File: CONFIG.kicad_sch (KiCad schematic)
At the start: 26 parts, among them IC1 ECP5-BGA256, J1 Conn_ARM_JTAG_SWD_10, U5 AT25SF081-SSHD-X

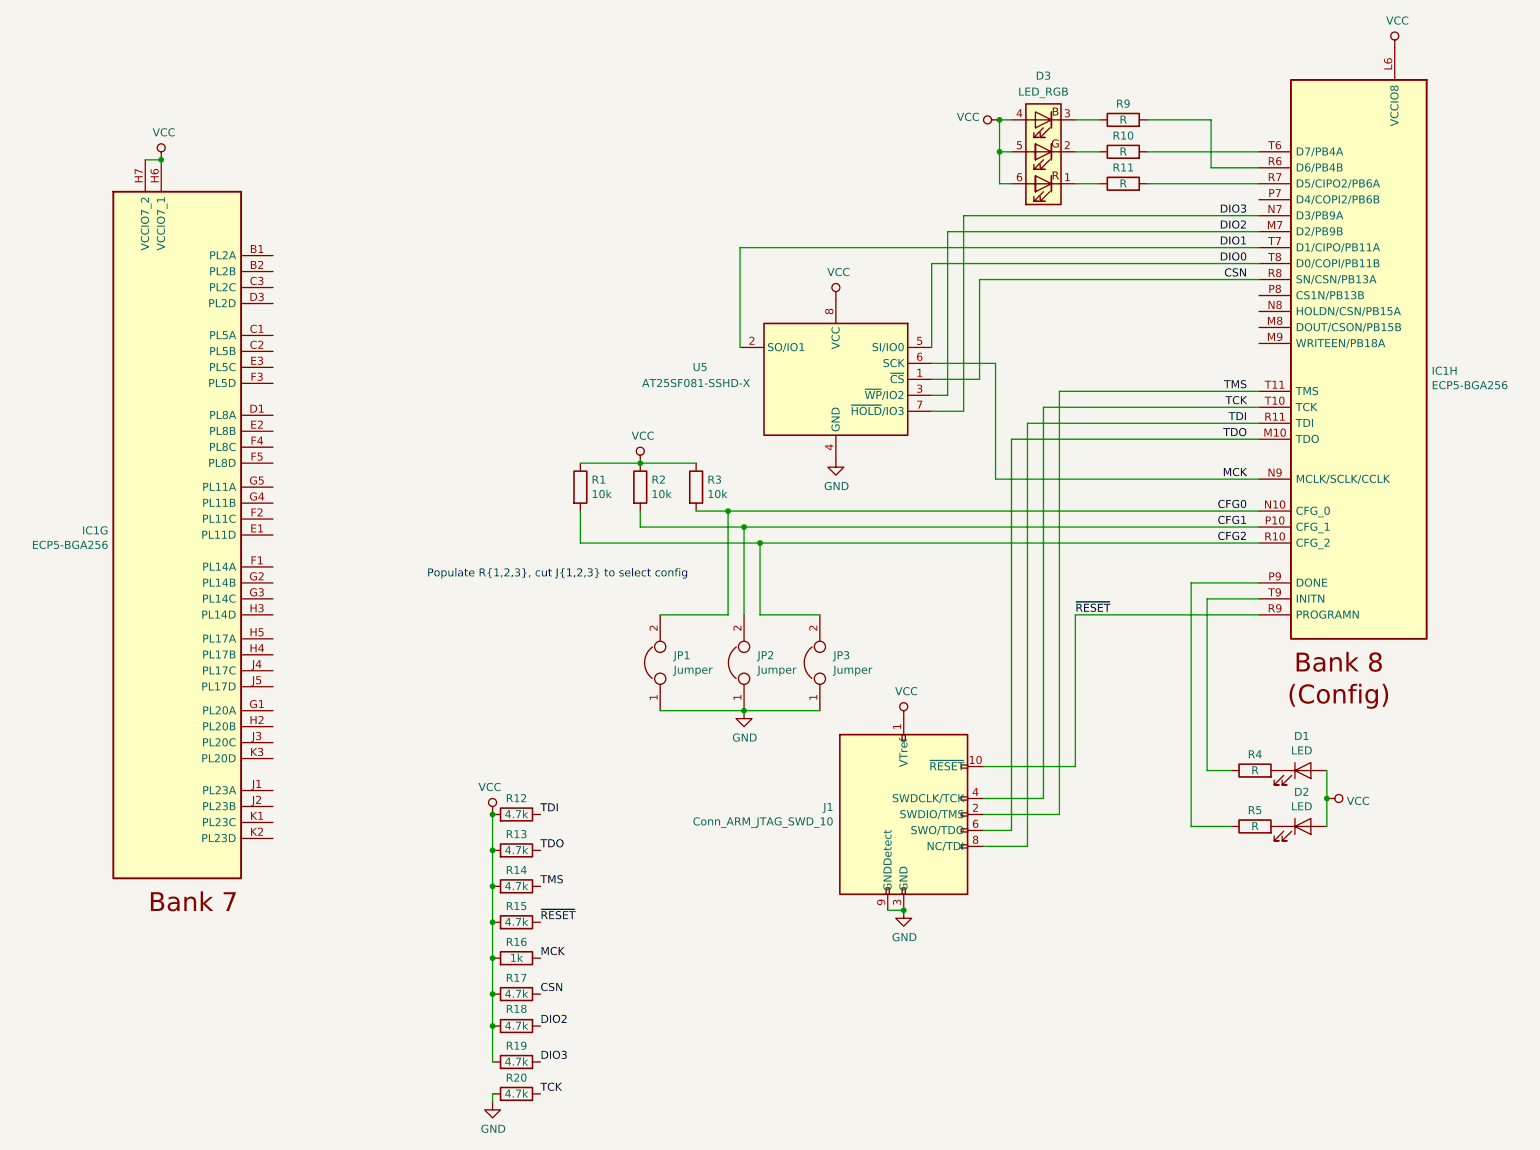
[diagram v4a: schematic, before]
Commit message: Change oscillator to SI5315, change RGB LED
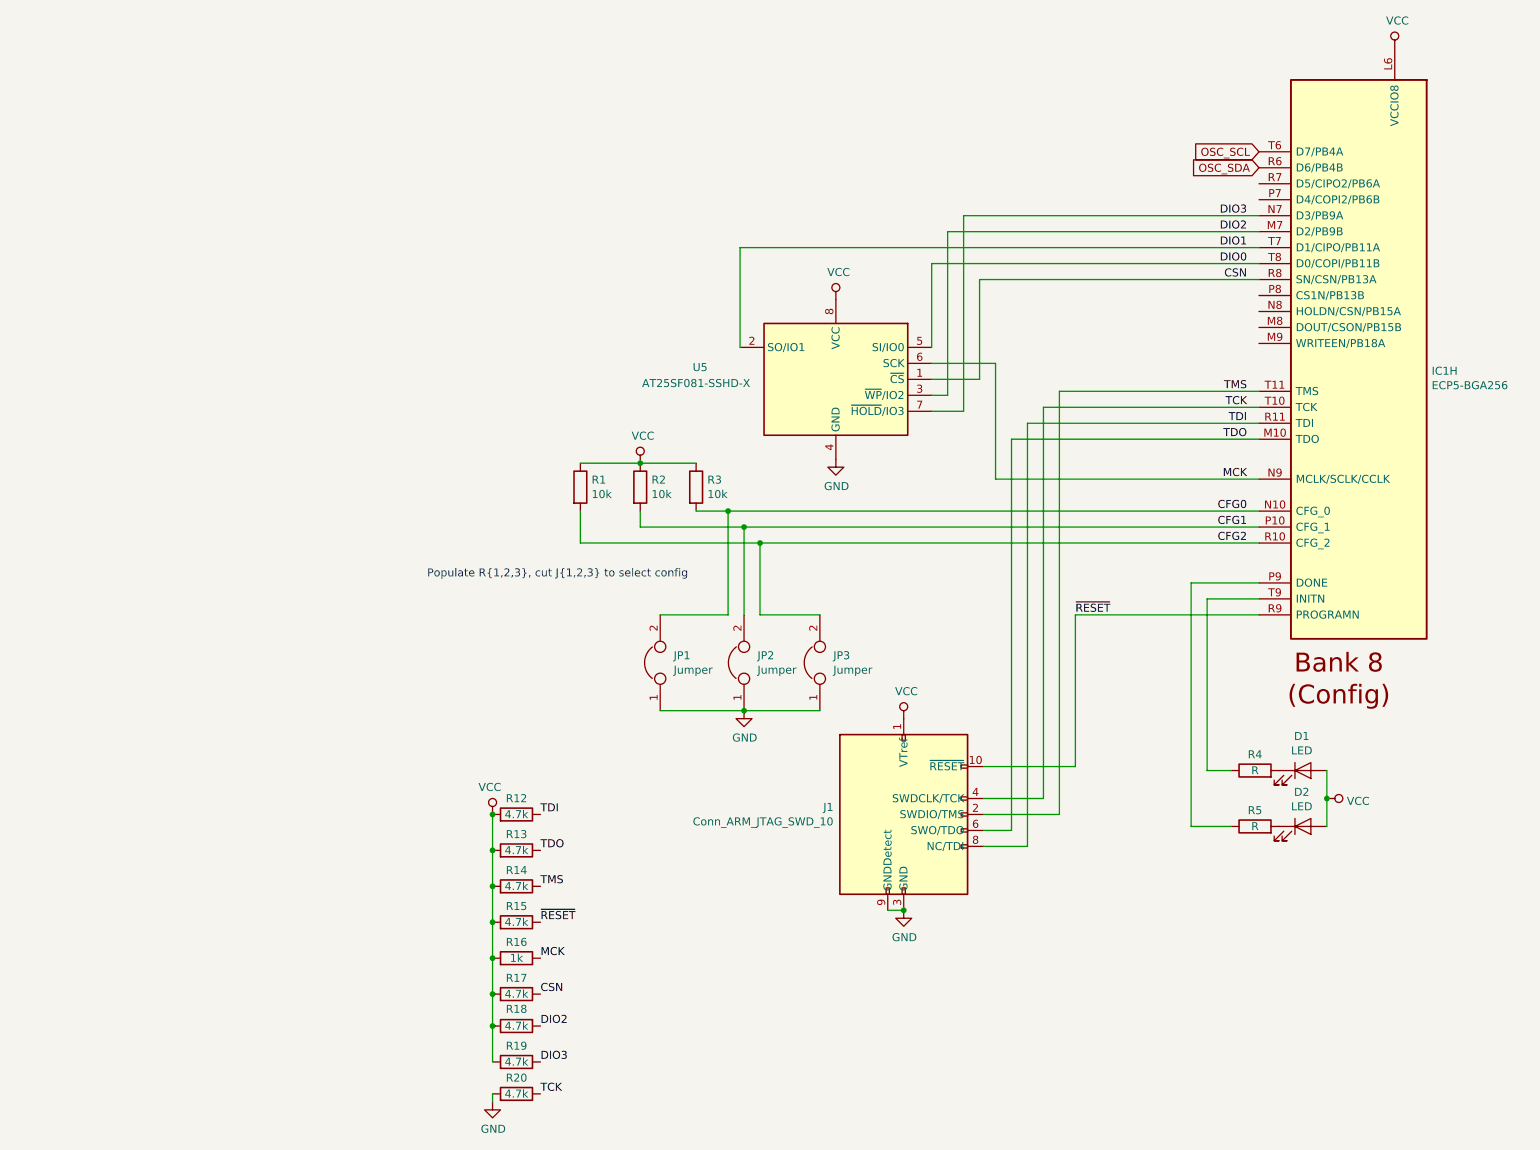
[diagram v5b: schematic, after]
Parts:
- removed D3: LED_RGB, mini-mipi:FM-Z3535RGBA-SH, symbol Device:LED_RGB
- removed unit 7 of IC1
- removed R10, R11, R9: R, Resistor_SMD:R_0402_1005Metric, symbol Device:R
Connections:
- net OSC_SDA: now reaches IC1.R6 (D6/PB4B)
- net OSC_SCL: now reaches IC1.T6 (D7/PB4A)
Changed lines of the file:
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@@
-(kicad_sch (version 20200714) (host eeschema "5.99.0-unknown-9f20c61~102~ubuntu20.04.1")
+(kicad_sch (version 20200714) (host eeschema "5.99.0-unknown-20c1492~102~ubuntu20.04.1")
   (page 4 6)
   (paper "A4")
-  (junction (at 40.005 36.83) (diameter 0) (color 0 0 0 0))
   (junction (at 92.71 140.97) (diameter 0) (color 0 0 0 0))
   (junction (at 92.71 146.685) (diameter 0) (color 0 0 0 0))
@@
   (junction (at 135.255 97.79) (diameter 0) (color 0 0 0 0))
   (junction (at 158.115 156.21) (diameter 0) (color 0 0 0 0))
-  (junction (at 173.355 30.48) (diameter 0) (color 0 0 0 0))
-  (junction (at 173.355 35.56) (diameter 0) (color 0 0 0 0))
   (junction (at 225.425 138.43) (diameter 0) (color 0 0 0 0))
-  (wire (pts (xy 37.465 36.83) (xy 40.005 36.83))
-    (stroke (width 0) (type solid) (color 0 0 0 0))
-  )
   (wire (pts (xy 92.71 140.97) (xy 92.71 146.685))
     (stroke (width 0) (type solid) (color 0 0 0 0))
@@
     (stroke (width 0) (type solid) (color 0 0 0 0))
   )
-  (wire (pts (xy 173.355 30.48) (xy 173.355 35.56))
-    (stroke (width 0) (type solid) (color 0 0 0 0))
-  )
-  (wire (pts (xy 173.355 30.48) (xy 175.26 30.48))
-    (stroke (width 0) (type solid) (color 0 0 0 0))
-  )
-  (wire (pts (xy 173.355 35.56) (xy 173.355 40.64))
-    (stroke (width 0) (type solid) (color 0 0 0 0))
-  )
-  (wire (pts (xy 173.355 35.56) (xy 175.26 35.56))
-    (stroke (width 0) (type solid) (color 0 0 0 0))
-  )
-  (wire (pts (xy 173.355 40.64) (xy 175.26 40.64))
-    (stroke (width 0) (type solid) (color 0 0 0 0))
-  )
   (wire (pts (xy 175.26 81.28) (xy 214.63 81.28))
     (stroke (width 0) (type solid) (color 0 0 0 0))
@@
     (stroke (width 0) (type solid) (color 0 0 0 0))
   )
-  (wire (pts (xy 185.42 30.48) (xy 189.23 30.48))
-    (stroke (width 0) (type solid) (color 0 0 0 0))
-  )
-  (wire (pts (xy 185.42 35.56) (xy 189.23 35.56))
-    (stroke (width 0) (type solid) (color 0 0 0 0))
-  )
-  (wire (pts (xy 185.42 40.64) (xy 189.23 40.64))
-    (stroke (width 0) (type solid) (color 0 0 0 0))
-  )
   (wire (pts (xy 185.42 109.22) (xy 185.42 133.35))
     (stroke (width 0) (type solid) (color 0 0 0 0))
@@
     (stroke (width 0) (type solid) (color 0 0 0 0))
   )
-  (wire (pts (xy 196.85 30.48) (xy 207.01 30.48))
-    (stroke (width 0) (type solid) (color 0 0 0 0))
-  )
-  (wire (pts (xy 196.85 35.56) (xy 214.63 35.56))
-    (stroke (width 0) (type solid) (color 0 0 0 0))
-  )
-  (wire (pts (xy 196.85 40.64) (xy 214.63 40.64))
-    (stroke (width 0) (type solid) (color 0 0 0 0))
-  )
   (wire (pts (xy 203.835 104.14) (xy 214.63 104.14))
     (stroke (width 0) (type solid) (color 0 0 0 0))
@@
     (stroke (width 0) (type solid) (color 0 0 0 0))
   )
-  (wire (pts (xy 207.01 30.48) (xy 207.01 38.1))
-    (stroke (width 0) (type solid) (color 0 0 0 0))
-  )
-  (wire (pts (xy 207.01 38.1) (xy 214.63 38.1))
-    (stroke (width 0) (type solid) (color 0 0 0 0))
-  )
   (wire (pts (xy 214.63 92.71) (xy 130.175 92.71))
     (stroke (width 0) (type solid) (color 0 0 0 0))
@@
     (effects (font (size 1.27 1.27)) (justify right bottom))
   )
-  (symbol (lib_id "power:VCC") (at 40.005 36.83 0) (unit 1)
-    (in_bom yes) (on_board yes)
-    (property "Reference" "#PWR0106" (id 0) (at 40.005 40.64 0)
-      (effects (font (size 1.27 1.27)) hide)
-    )
-    (property "Value" "VCC" (id 1) (at 40.4368 32.5056 0))
-    (property "Footprint" "" (id 2) (at 40.005 36.83 0)
-      (effects (font (size 1.27 1.27)) hide)
-    )
-    (property "Datasheet" "" (id 3) (at 40.005 36.83 0)
-      (effects (font (size 1.27 1.27)) hide)
-    )
+  (global_label "OSC_SCL" (shape input) (at 214.63 35.56 180)
+    (effects (font (size 1.27 1.27)) (justify right))
+  )
+  (global_label "OSC_SDA" (shape input) (at 214.63 38.1 180)
+    (effects (font (size 1.27 1.27)) (justify right))
   )
   (symbol (lib_id "power:VCC") (at 92.71 140.97 0) (mirror y) (unit 1)
@@
     )
     (property "Datasheet" "" (id 3) (at 158.115 125.73 0)
-      (effects (font (size 1.27 1.27)) hide)
-    )
-  )
-  (symbol (lib_id "power:VCC") (at 173.355 30.48 90) (unit 1)
-    (in_bom yes) (on_board yes)
-    (property "Reference" "#PWR0141" (id 0) (at 177.165 30.48 0)
-      (effects (font (size 1.27 1.27)) hide)
-    )
-    (property "Value" "VCC" (id 1) (at 170.1799 30.0482 90)
-      (effects (font (size 1.27 1.27)) (justify left))
-    )
-    (property "Footprint" "" (id 2) (at 173.355 30.48 0)
-      (effects (font (size 1.27 1.27)) hide)
-    )
-    (property "Datasheet" "" (id 3) (at 173.355 30.48 0)
       (effects (font (size 1.27 1.27)) hide)
     )
@@
     )
   )
-  (symbol (lib_id "Device:R") (at 193.04 30.48 90) (unit 1)
-    (in_bom yes) (on_board yes)
-    (property "Reference" "R9" (id 0) (at 193.04 27.94 90))
-    (property "Value" "R" (id 1) (at 193.04 30.48 90))
-    (property "Footprint" "Resistor_SMD:R_0402_1005Metric" (id 2) (at 193.04 32.258 90)
-      (effects (font (size 1.27 1.27)) hide)
-    )
-    (property "Datasheet" "~" (id 3) (at 193.04 30.48 0)
-      (effects (font (size 1.27 1.27)) hide)
-    )
-  )
-  (symbol (lib_id "Device:R") (at 193.04 35.56 90) (unit 1)
-    (in_bom yes) (on_board yes)
-    (property "Reference" "R10" (id 0) (at 193.04 33.02 90))
-    (property "Value" "R" (id 1) (at 193.04 35.56 90))
-    (property "Footprint" "Resistor_SMD:R_0402_1005Metric" (id 2) (at 193.04 37.338 90)
-      (effects (font (size 1.27 1.27)) hide)
-    )
-    (property "Datasheet" "~" (id 3) (at 193.04 35.56 0)
-      (effects (font (size 1.27 1.27)) hide)
-    )
-  )
-  (symbol (lib_id "Device:R") (at 193.04 40.64 90) (unit 1)
-    (in_bom yes) (on_board yes)
-    (property "Reference" "R11" (id 0) (at 193.04 38.1 90))
-    (property "Value" "R" (id 1) (at 193.04 40.64 90))
-    (property "Footprint" "Resistor_SMD:R_0402_1005Metric" (id 2) (at 193.04 42.418 90)
-      (effects (font (size 1.27 1.27)) hide)
-    )
-    (property "Datasheet" "~" (id 3) (at 193.04 40.64 0)
-      (effects (font (size 1.27 1.27)) hide)
-    )
-  )
   (symbol (lib_id "Device:R") (at 213.995 133.985 90) (unit 1)
     (in_bom yes) (on_board yes)
@@
     )
   )
-  (symbol (lib_id "Device:LED_RGB") (at 180.34 35.56 180) (unit 1)
-    (in_bom yes) (on_board yes)
-    (property "Reference" "D3" (id 0) (at 180.34 23.495 0))
-    (property "Value" "LED_RGB" (id 1) (at 180.34 26.035 0))
-    (property "Footprint" "mini-mipi:FM-Z3535RGBA-SH" (id 2) (at 180.34 34.29 0)
-      (effects (font (size 1.27 1.27)) hide)
-    )
-    (property "Datasheet" "~" (id 3) (at 180.34 34.29 0)
-      (effects (font (size 1.27 1.27)) hide)
-    )
-  )
   (symbol (lib_id "Connector:Conn_ARM_JTAG_SWD_10") (at 158.115 140.97 0) (unit 1)
     (in_bom yes) (on_board yes)
@@
       (effects (font (size 1.27 1.27)) (justify left) hide)
     )
-  )
-  (symbol (lib_name "mini_mipi:ECP5-BGA256_1") (lib_id "mini_mipi:ECP5-BGA256") (at 32.385 41.91 0) (unit 7)
-    (in_bom yes) (on_board yes)
-    (property "Reference" "IC1" (id 0) (at 31.5976 95.8319 0)
-      (effects (font (size 1.27 1.27)) (justify right))
-    )
-    (property "Value" "ECP5-BGA256" (id 1) (at 31.5976 98.1306 0)
-      (effects (font (size 1.27 1.27)) (justify right))
-    )
-    (property "Footprint" "mini-mipi:BGA256C80P16X16_1400X1400X170" (id 2) (at -48.895 -45.72 0)
-      (effects (font (size 1.27 1.27)) (justify left) hide)
-    )
-    (property "Datasheet" "" (id 3) (at -60.325 -69.85 0)
-      (effects (font (size 1.27 1.27)) (justify left) hide)
-    )
-    (property "Description" "FPGA - Field Programmable Gate Array ECP5; 12k LUTs; 1.1V" (id 4) (at -60.325 -67.31 0)
-      (effects (font (size 1.27 1.27)) (justify left) hide)
-    )
-    (property "Height" "1.7" (id 5) (at -60.325 -76.2 0)
-      (effects (font (size 1.27 1.27)) (justify left) hide)
-    )
-    (property "Manufacturer_Name" "Lattice" (id 6) (at -59.055 -91.44 0)
-      (effects (font (size 1.27 1.27)) (justify left) hide)
-    )
-    (property "Manufacturer_Part_Number" "LFE5U-12F-6BG256C" (id 7) (at -59.055 -88.9 0)
-      (effects (font (size 1.27 1.27)) (justify left) hide)
-    )
-    (property "Mouser Part Number" "842-LFE5U12F6BG256C" (id 8) (at -42.545 -55.88 0)
-      (effects (font (size 1.27 1.27)) (justify left) hide)
-    )
-    (property "Mouser Price/Stock" "https://www.mouser.com/Search/Refine.aspx?Keyword=842-LFE5U12F6BG256C" (id 9) (at -51.435 -52.07 0)
-      (effects (font (size 1.27 1.27)) (justify left) hide)
-    )

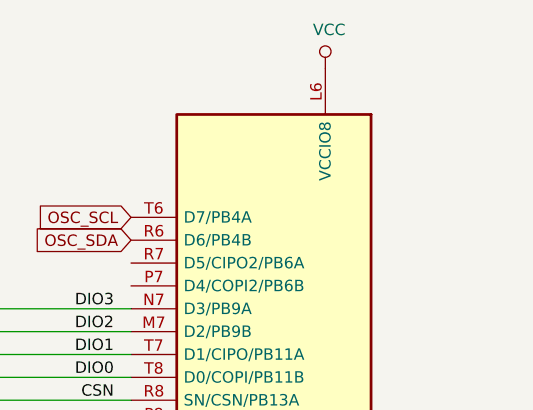
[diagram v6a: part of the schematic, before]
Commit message: Improve decoupling
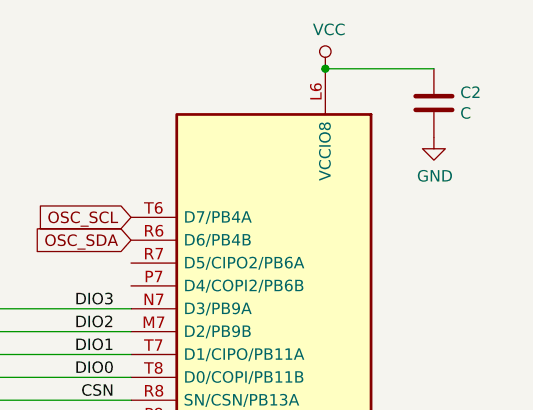
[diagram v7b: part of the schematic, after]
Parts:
- added C2: C, Capacitor_SMD:C_0402_1005Metric, symbol Device:C
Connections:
- net GND: now also C2.2
- net VCC: now also C2.1
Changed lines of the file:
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@@
 (kicad_sch (version 20200714) (host eeschema "5.99.0-unknown-a61ea1f~102~ubuntu20.04.1")
-  (page 1 6)
+  (page 4 6)
   (paper "A4")
   (junction (at 92.71 140.97) (diameter 0) (color 0 0 0 0))
@@
   (junction (at 158.115 156.21) (diameter 0) (color 0 0 0 0))
   (junction (at 225.425 138.43) (diameter 0) (color 0 0 0 0))
+  (junction (at 236.22 19.05) (diameter 0) (color 0 0 0 0))
   (wire (pts (xy 92.71 140.97) (xy 92.71 146.685))
     (stroke (width 0) (type solid) (color 0 0 0 0))
@@
   )
   (wire (pts (xy 225.425 138.43) (xy 225.425 142.875))
+    (stroke (width 0) (type solid) (color 0 0 0 0))
+  )
+  (wire (pts (xy 236.22 19.05) (xy 248.285 19.05))
     (stroke (width 0) (type solid) (color 0 0 0 0))
   )
@@
     )
     (property "Datasheet" "" (id 3) (at 158.115 156.21 0)
+      (effects (font (size 1.27 1.27)) hide)
+    )
+  )
+  (symbol (lib_id "power:GND") (at 248.285 26.67 0) (unit 1)
+    (in_bom yes) (on_board yes)
+    (property "Reference" "#PWR0153" (id 0) (at 248.285 33.02 0)
+      (effects (font (size 1.27 1.27)) hide)
+    )
+    (property "Value" "GND" (id 1) (at 248.3993 30.9944 0))
+    (property "Footprint" "" (id 2) (at 248.285 26.67 0)
+      (effects (font (size 1.27 1.27)) hide)
+    )
+    (property "Datasheet" "" (id 3) (at 248.285 26.67 0)
       (effects (font (size 1.27 1.27)) hide)
     )
@@
       (effects (font (size 1.27 1.27)) hide)
     )
+  )
+  (symbol (lib_id "Device:C") (at 248.285 22.86 0) (unit 1)
+    (in_bom yes) (on_board yes)
+    (property "Reference" "C2" (id 0) (at 251.2061 21.7106 0)
+      (effects (font (size 1.27 1.27)) (justify left))
+    )
+    (property "Value" "C" (id 1) (at 251.2061 24.0093 0)
+      (effects (font (size 1.27 1.27)) (justify left))
+    )
+    (property "Footprint" "Capacitor_SMD:C_0402_1005Metric" (id 2) (at 249.2502 26.67 0)
+      (effects (font (size 1.27 1.27)) hide)
+    )
+    (property "Datasheet" "~" (id 3) (at 248.285 22.86 0)
+      (effects (font (size 1.27 1.27)) hide)
+    )
